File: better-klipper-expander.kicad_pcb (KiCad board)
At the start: 4 copper layers, 105 x 30 mm, 95 parts, among them J1 24V IN, J10 TH1, J11 VFAN_SEL1, J12 Neopixel, J13 VFAN_SEL2, J2 USB4105-GF-A, J3 FAN0, J4 FAN1, J5 FAN2, J6 TH0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

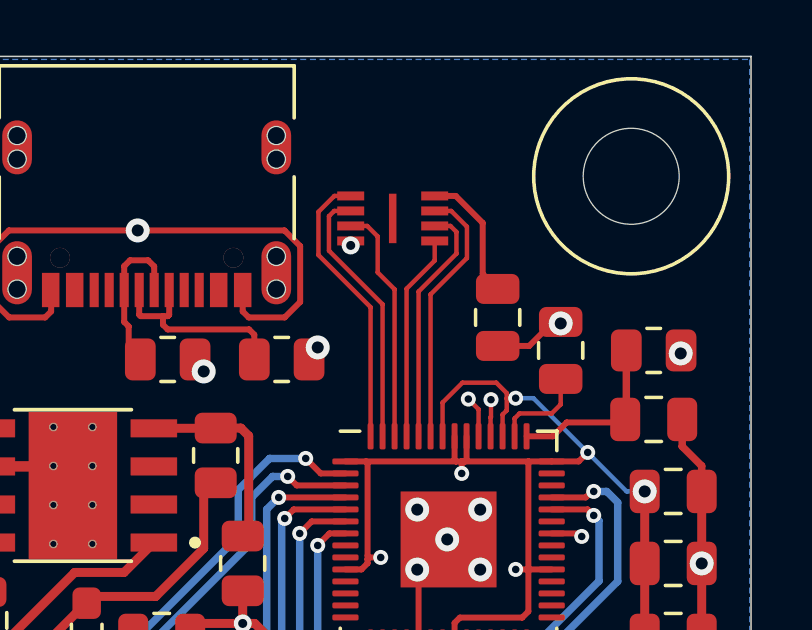
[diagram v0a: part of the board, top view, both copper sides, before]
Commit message: Move Flash Closer to RP2040
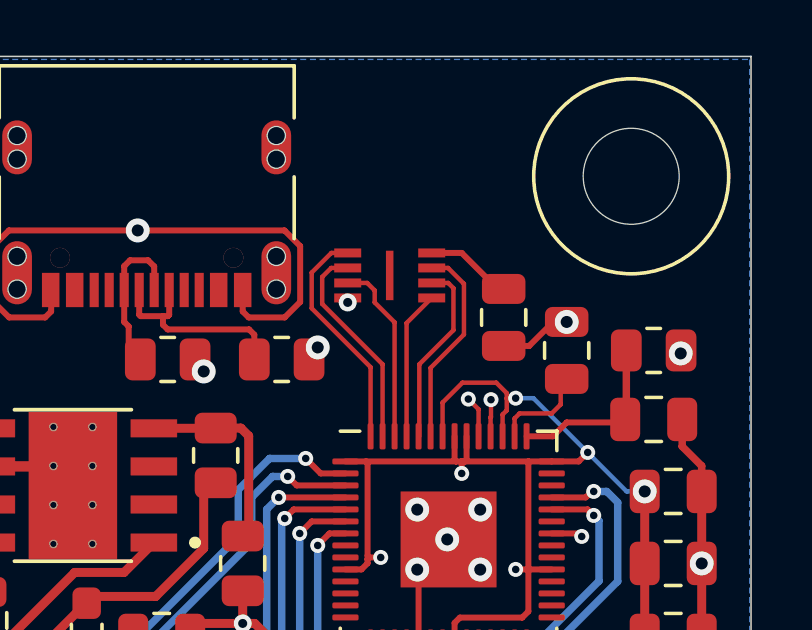
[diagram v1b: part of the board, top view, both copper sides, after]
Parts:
- moved U1 1.90 mm to (181.0, 84.8)
- moved C14 0.20 mm to (186.9, 87.3)
- moved C15 0.20 mm to (184.8, 86.2)
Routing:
- net SD3: track 8.78 -> 6.84 mm
- net SD0: track 6.90 -> 4.96 mm
- net CLK: track 8.14 -> 6.21 mm
- net SD2: track 7.94 -> 6.14 mm
- net CS: track 9.50 -> 7.74 mm
- net SD1: track 8.88 -> 7.12 mm
- net Net-(C15-Pad1): track 4.38 -> 2.90 mm
